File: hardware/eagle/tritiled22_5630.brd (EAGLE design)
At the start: 27.9 x 27.9 mm, 15 parts, among them Q1 ZXMN3B01FTA, Q2 DMG2305UX, SW1 SMD_SWITCH, U1 PIC12LF1571

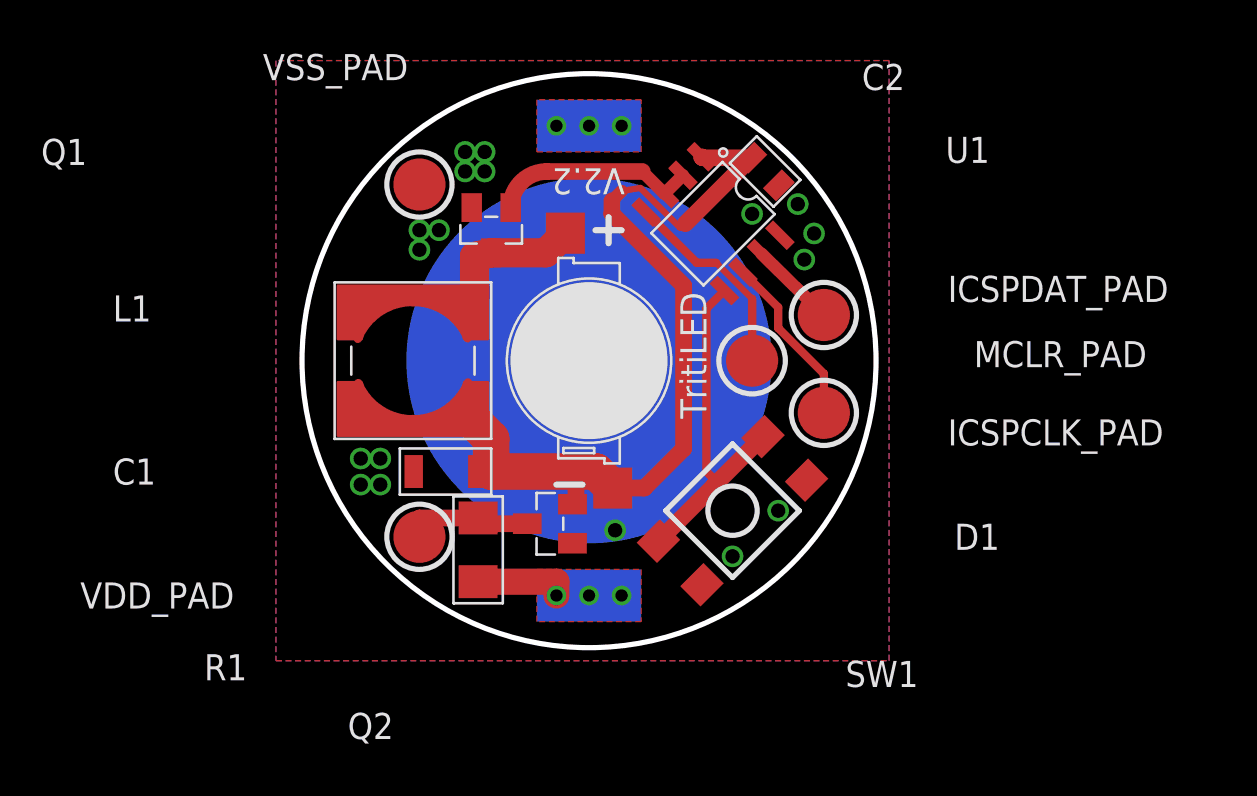
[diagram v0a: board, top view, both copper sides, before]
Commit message: Added new LED eiditons: 5630, Luxeon C, Luxeon Z fixed inconsistent C2 value: now should be 100n everywhere
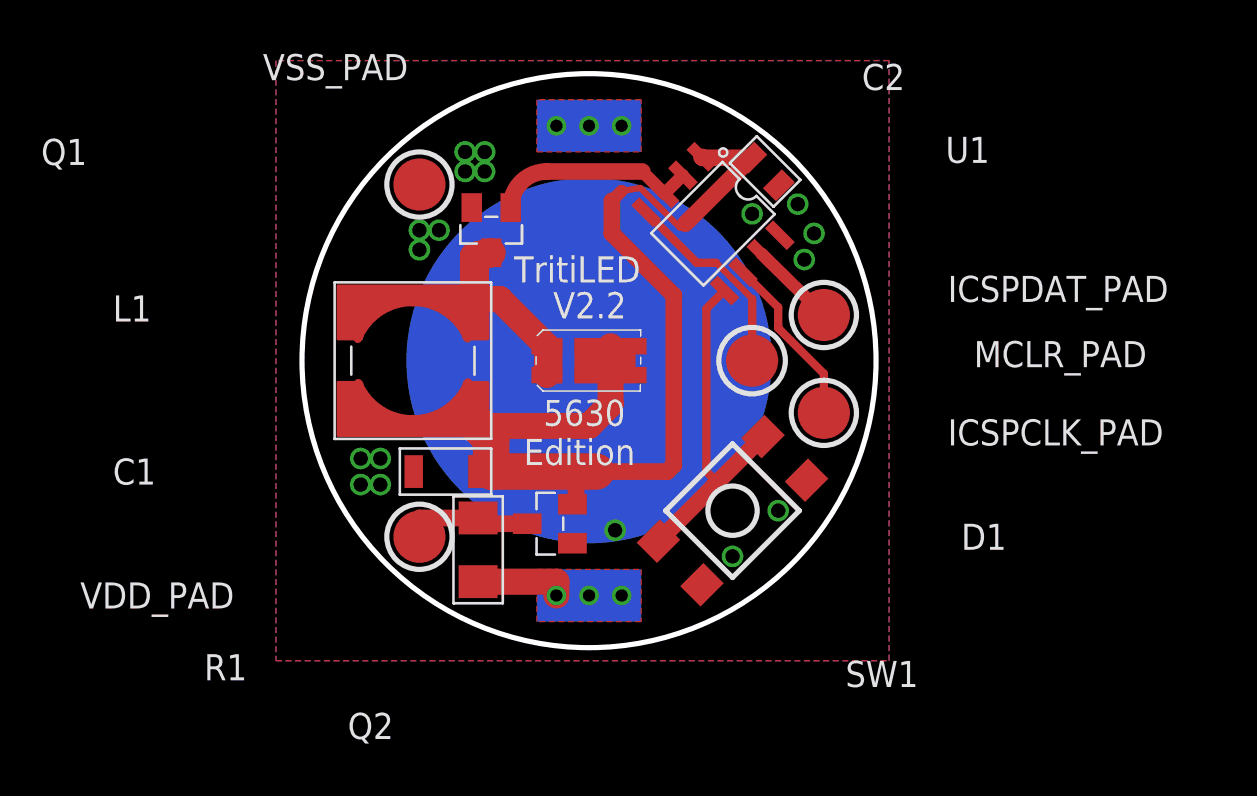
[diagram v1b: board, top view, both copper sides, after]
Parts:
- D1: value Chanzon 3W -> 5630; device tritiled:LED_3W -> tritiled:LED_5630
- turned D1 to 180 degrees
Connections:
- net +3.3V: now also D1.C@1, D1.C@2; no longer D1.C
- net N$5: now also D1.A@1, D1.A@2; no longer D1.A
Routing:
- net +3.3V: track 41.2 -> 50.7 mm
- net N$5: track 6.91 -> 8.78 mm
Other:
- board text added: "5630"
- board text added: "Edition"
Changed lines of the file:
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@@
 <plain>
 <circle x="15.24" y="14.605" radius="13.97" width="0.254" layer="20"/>
-<circle x="15.24" y="14.605" radius="3.82320625" width="0" layer="21"/>
 <circle x="6.985" y="6.0325" radius="1.5875" width="0.254" layer="21"/>
 <circle x="6.985" y="23.1775" radius="1.5875" width="0.254" layer="21"/>
@@
 <circle x="26.67" y="16.8275" radius="1.5875" width="0.254" layer="21"/>
 <circle x="23.1775" y="14.605" radius="1.6189375" width="0.254" layer="21"/>
-<text x="19.685" y="17.93875" size="1.27" layer="21" font="vector" ratio="13" rot="R270">TritiLED</text>
-<text x="16.98625" y="23.97125" size="1.27" layer="21" font="vector" ratio="13" rot="SR180">V2.2</text>
+<text x="11.58875" y="18.415" size="1.27" layer="21" font="vector" ratio="13">TritiLED</text>
+<text x="13.49375" y="16.66875" size="1.27" layer="21" font="vector" ratio="13" rot="SR0">V2.2</text>
 <wire x1="11.43" y1="26.035" x2="11.43" y2="3.175" width="3.81" layer="22" curve="143.130102" cap="flat"/>
 <wire x1="19.05" y1="26.035" x2="19.05" y2="3.175" width="3.81" layer="22" curve="-143.130102" cap="flat"/>
@@
 <wire x1="14.9225" y1="1.27" x2="15.5575" y2="1.27" width="0.3048" layer="22"/>
 <wire x1="15.24" y1="1.5875" x2="15.24" y2="0.9525" width="0.3048" layer="22"/>
-<wire x1="13.6525" y1="8.5725" x2="14.9225" y2="8.5725" width="0.3048" layer="21"/>
-<wire x1="15.5575" y1="20.955" x2="16.8275" y2="20.955" width="0.3048" layer="21"/>
-<wire x1="16.1925" y1="21.59" x2="16.1925" y2="20.32" width="0.3048" layer="21"/>
 <dimension x1="9.8425" y1="5.3975" x2="-0.3175" y2="-0.9525" x3="-0.9525" y3="-1.27" textsize="1.778" layer="48" dtype="leader"/>
 <dimension x1="8.255" y1="9.2075" x2="-4.445" y2="8.5725" x3="-4.445" y3="8.5725" textsize="1.778" layer="48" dtype="leader"/>
@@
 <dimension x1="15.24" y1="14.605" x2="32.385" y2="5.08" x3="32.385" y3="5.08" textsize="1.778" layer="48" dtype="leader"/>
 <dimension x1="6.985" y1="6.0325" x2="-0.9525" y2="3.4925" x3="-0.9525" y3="3.4925" textsize="1.778" layer="48" dtype="leader"/>
+<text x="13.0175" y="11.43" size="1.27" layer="21" ratio="13">5630</text>
+<text x="12.065" y="9.525" size="1.27" layer="21" ratio="13">Edition</text>
 </plain>
 <attributes>
@@
 <attribute name="VALUE" x="-7.9375" y="14.605" size="1.27" layer="27"/>
 </element>
-<element name="D1" library="tritiled" package="LED_3W" value="Chanzon 3W" x="15.24" y="14.605" smashed="yes" rot="R90">
-<attribute name="NAME" x="33.02" y="5.3975" size="1.27" layer="25"/>
-<attribute name="VALUE" x="33.02" y="3.4925" size="1.27" layer="27"/>
+<element name="D1" library="tritiled" package="LED_5630" value="5630" x="15.24" y="14.605" smashed="yes" rot="R180">
+<attribute name="NAME" x="35.56" y="6.6675" size="1.27" layer="25" rot="R180"/>
+<attribute name="VALUE" x="33.3375" y="3.175" size="1.27" layer="27"/>
 </element>
 <element name="B1" library="tritiled" package="CR2032_BAT-HLD_001" value="BAT-HLD-001_CR2032" x="15.24" y="14.605" rot="MR270"/>
@@
 <signal name="N$5">
 <contactref element="L1" pad="P$2"/>
-<contactref element="D1" pad="A"/>
+<contactref element="D1" pad="A@1"/>
 <contactref element="Q1" pad="3"/>
-<wire x1="14.09" y1="20.805" x2="13.14" y2="19.855" width="1.4224" layer="1"/>
-<wire x1="13.14" y1="19.855" x2="10.4775" y2="19.855" width="1.4224" layer="1"/>
 <wire x1="10.4775" y1="19.855" x2="9.6675" y2="19.68" width="1.4224" layer="1"/>
 <wire x1="9.6675" y1="19.68" x2="9.6675" y2="17.605" width="1.4224" layer="1"/>
+<contactref element="D1" pad="A@2"/>
+<wire x1="9.6675" y1="17.605" x2="10.89" y2="17.605" width="1.27" layer="1"/>
+<wire x1="10.89" y1="17.605" x2="13.19" y2="15.305" width="1.27" layer="1"/>
+<wire x1="13.19" y1="15.305" x2="13.19" y2="13.905" width="1.27" layer="1"/>
 </signal>
 <signal name="+3.3V">
 <contactref element="L1" pad="P$1"/>
-<contactref element="D1" pad="C"/>
+<contactref element="D1" pad="C@1"/>
 <wire x1="9.6675" y1="11.605" x2="9.755" y2="11.5175" width="1.778" layer="1"/>
-<wire x1="16.66" y1="8.405" x2="16.39" y2="8.405" width="0.8128" layer="1"/>
-<wire x1="16.35125" y1="21.74875" x2="19.84375" y2="18.25625" width="0.8128" layer="1"/>
-<wire x1="19.84375" y1="18.25625" x2="19.84375" y2="10.31875" width="0.8128" layer="1"/>
-<wire x1="19.84375" y1="10.31875" x2="17.93" y2="8.405" width="0.8128" layer="1"/>
-<wire x1="17.93" y1="8.405" x2="16.39" y2="8.405" width="0.8128" layer="1"/>
 <contactref element="Q2" pad="2"/>
 <contactref element="C1" pad="P$1"/>
 <contactref element="C2" pad="P$1"/>
-<wire x1="16.39" y1="8.405" x2="15.5875" y2="9.2075" width="1.778" layer="1"/>
 <wire x1="15.5875" y1="9.2075" x2="14.605" y2="9.2075" width="1.778" layer="1"/>
 <wire x1="14.605" y1="9.2075" x2="10.4775" y2="9.2075" width="1.778" layer="1"/>
@@
 <wire x1="17.73555" y1="23.0124" x2="16.8275" y2="22.86" width="0.3048" layer="1"/>
 <wire x1="16.8275" y1="22.86" x2="16.35125" y2="22.38375" width="0.6096" layer="1"/>
-<wire x1="16.35125" y1="22.38375" x2="16.35125" y2="21.74875" width="0.8128" layer="1"/>
 <wire x1="14.435" y1="7.6175" x2="14.605" y2="7.6175" width="0.8128" layer="1"/>
 <wire x1="14.605" y1="7.6175" x2="14.605" y2="9.2075" width="0.8128" layer="1"/>
 <wire x1="9.805" y1="9.2075" x2="10.4775" y2="9.2075" width="0.6096" layer="1"/>
+<wire x1="16.35125" y1="20.79625" x2="19.3675" y2="17.78" width="0.8128" layer="1"/>
+<wire x1="19.3675" y1="17.78" x2="19.3675" y2="9.525" width="0.8128" layer="1"/>
+<wire x1="19.3675" y1="9.525" x2="19.05" y2="9.2075" width="0.8128" layer="1"/>
+<wire x1="19.05" y1="9.2075" x2="15.5875" y2="9.2075" width="0.8128" layer="1"/>
+<wire x1="16.35125" y1="22.38375" x2="16.35125" y2="20.79625" width="0.8128" layer="1"/>
+<wire x1="10.1275" y1="12.065" x2="9.6675" y2="11.605" width="0.254" layer="1"/>
+<contactref element="D1" pad="C@2"/>
+<wire x1="16.29" y1="15.305" x2="16.29" y2="13.905" width="1.27" layer="1"/>
+<wire x1="16.29" y1="13.905" x2="16.29" y2="12.48" width="1.27" layer="1"/>
+<wire x1="16.29" y1="12.48" x2="15.24" y2="11.43" width="1.27" layer="1"/>
+<wire x1="15.24" y1="11.43" x2="9.8425" y2="11.43" width="1.27" layer="1"/>
+<wire x1="9.8425" y1="11.43" x2="9.6675" y2="11.605" width="1.27" layer="1"/>
 </signal>
 <signal name="N$7">
